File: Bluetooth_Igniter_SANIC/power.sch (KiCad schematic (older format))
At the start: 13 parts, among them J4 Screw_Terminal_01x02, U5 TPS63060

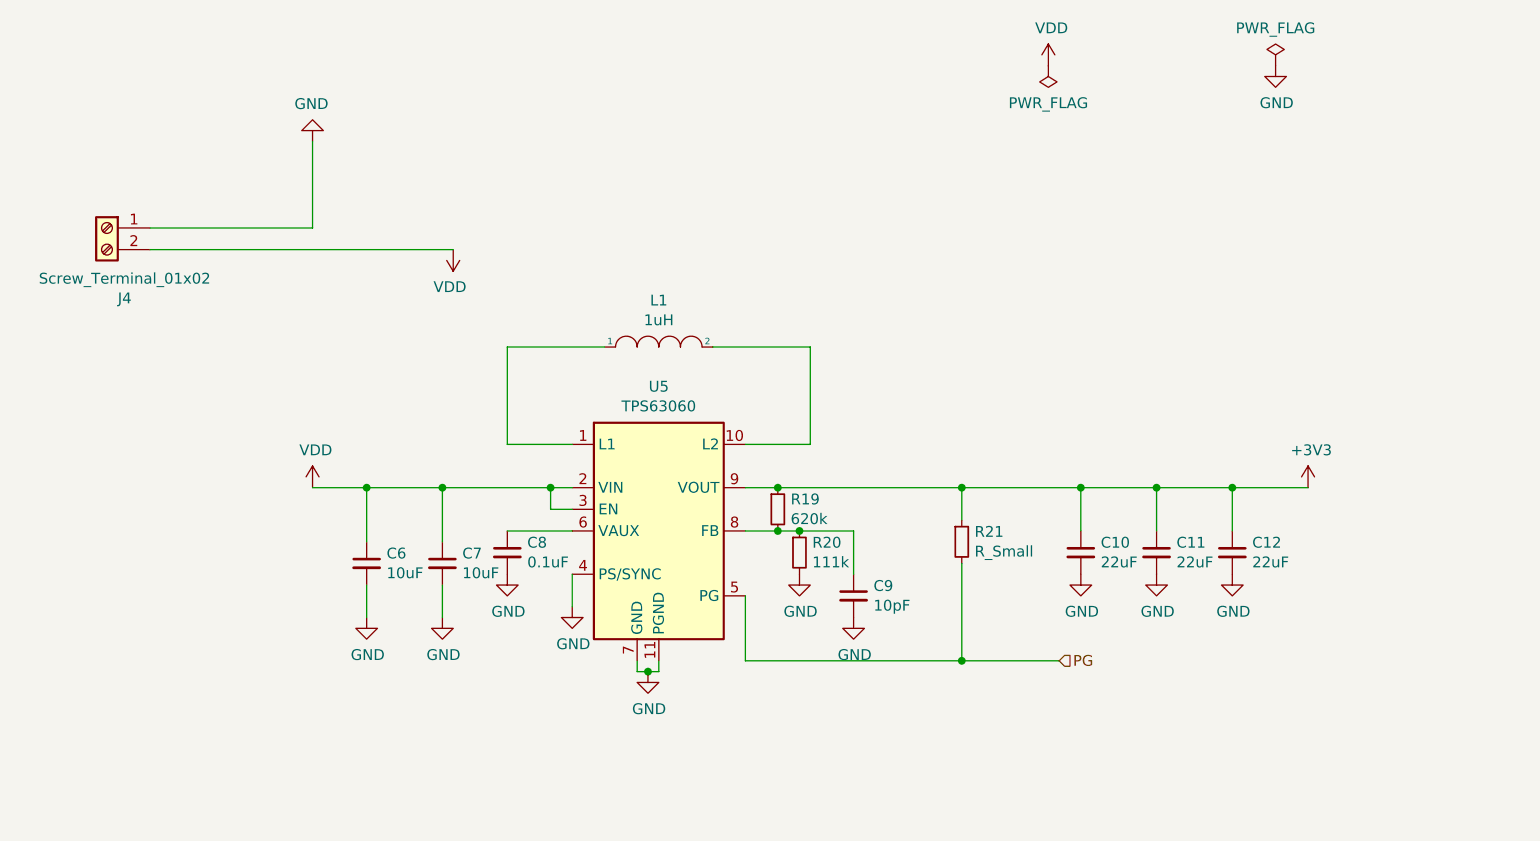
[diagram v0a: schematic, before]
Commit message: need to fit pin headers in
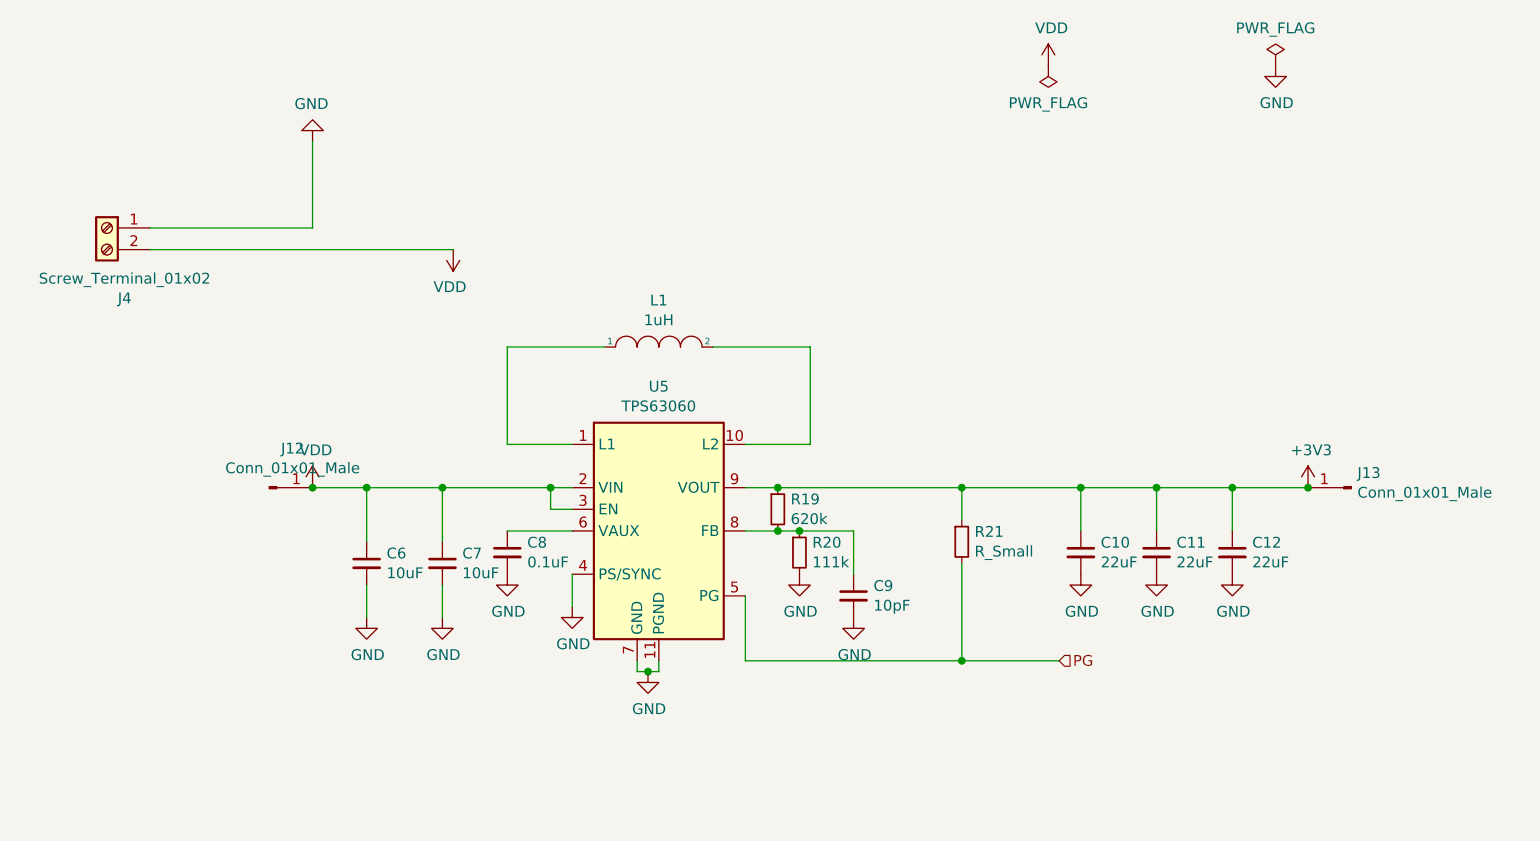
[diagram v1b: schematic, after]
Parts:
- added J12, J13: Conn_01x01_Male, Connector_PinHeader_2.54mm:PinHeader_1x01_P2.54mm_Vertical, symbol Connector:Conn_01x01_Male
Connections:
- net +3V3: now also J13.1 (Pin_1)
- net VDD: now also J12.1 (Pin_1)
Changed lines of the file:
@@
 	1    0    0    -1
 $EndComp
+$Comp
+L Connector:Conn_01x01_Male J12
+U 1 1 60D4A7BA
+P 3400 3050
+F 0 "J12" H 3508 3231 50  0000 C CNN
+F 1 "Conn_01x01_Male" H 3508 3140 50  0000 C CNN
+F 2 "Connector_PinHeader_2.54mm:PinHeader_1x01_P2.54mm_Vertical" H 3400 3050 50  0001 C CNN
+F 3 "~" H 3400 3050 50  0001 C CNN
+	1    3400 3050
+	1    0    0    -1
+$EndComp
+Connection ~ 3600 3050
+$Comp
+L Connector:Conn_01x01_Male J13
+U 1 1 60D4AF66
+P 8400 3050
+F 0 "J13" H 8372 2982 50  0000 R CNN
+F 1 "Conn_01x01_Male" H 8372 3073 50  0000 R CNN
+F 2 "Connector_PinHeader_2.54mm:PinHeader_1x01_P2.54mm_Vertical" H 8400 3050 50  0001 C CNN
+F 3 "~" H 8400 3050 50  0001 C CNN
+	1    8400 3050
+	-1   0    0    1
+$EndComp
+Connection ~ 8200 3050
 $EndSCHEMATC

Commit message: Before copper fills
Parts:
- removed J12, J13: Conn_01x01_Male, Connector_PinHeader_2.54mm:PinHeader_1x01_P2.54mm_Vertical, symbol Connector:Conn_01x01_Male
- added J10: Conn_01x02_Male, Connector_PinHeader_2.54mm:PinHeader_1x02_P2.54mm_Vertical, symbol Connector:Conn_01x02_Male
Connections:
- net +3V3: now also J10.2 (Pin_2)
- net VDD: now also J10.1 (Pin_1)
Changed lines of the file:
@@
 	1    0    0    -1
 $EndComp
-$Comp
-L Connector:Conn_01x01_Male J12
-U 1 1 60D4A7BA
-P 3400 3050
-F 0 "J12" H 3508 3231 50  0000 C CNN
-F 1 "Conn_01x01_Male" H 3508 3140 50  0000 C CNN
-F 2 "Connector_PinHeader_2.54mm:PinHeader_1x01_P2.54mm_Vertical" H 3400 3050 50  0001 C CNN
-F 3 "~" H 3400 3050 50  0001 C CNN
-	1    3400 3050
-	1    0    0    -1
-$EndComp
+Wire Wire Line
+	3600 3050 3600 4400
+Wire Wire Line
+	3600 4400 5850 4400
 Connection ~ 3600 3050
 $Comp
-L Connector:Conn_01x01_Male J13
-U 1 1 60D4AF66
-P 8400 3050
-F 0 "J13" H 8372 2982 50  0000 R CNN
-F 1 "Conn_01x01_Male" H 8372 3073 50  0000 R CNN
-F 2 "Connector_PinHeader_2.54mm:PinHeader_1x01_P2.54mm_Vertical" H 8400 3050 50  0001 C CNN
-F 3 "~" H 8400 3050 50  0001 C CNN
-	1    8400 3050
-	-1   0    0    1
+L Connector:Conn_01x02_Male J10
+U 1 1 60E29B82
+P 5850 4600
+F 0 "J10" V 6004 4412 50  0000 R CNN
+F 1 "Conn_01x02_Male" V 5913 4412 50  0000 R CNN
+F 2 "Connector_PinHeader_2.54mm:PinHeader_1x02_P2.54mm_Vertical" H 5850 4600 50  0001 C CNN
+F 3 "~" H 5850 4600 50  0001 C CNN
+	1    5850 4600
+	0    -1   -1   0
 $EndComp
+Wire Wire Line
+	8200 3050 8200 4400
+Wire Wire Line
+	8200 4400 5950 4400
 Connection ~ 8200 3050
 $EndSCHEMATC
